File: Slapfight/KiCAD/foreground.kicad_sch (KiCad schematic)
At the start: 27 parts, among them U2D 74LS374, U3B_? 74LS00, U3C_ 74LS86, U3D_ 74LS04, U3F 74LS157, U3G 74LS157, U3H 74LS157, U4B_ 74LS32, U4B_? 74LS32, U4C_ 74LS10, U4D 74LS157, U4F RAM_2016, U4G RAM_2016, U4H 74LS174, U4J 74LS245, U6&7D 74LS194, U6D 74LS194, U6F 27C64 - A77-04, U6G 27C64 - A77-03, U6H_ 74LS32, U6J 74LS245, U7D 74LS194, U7E 74LS194, U7F 74LS157

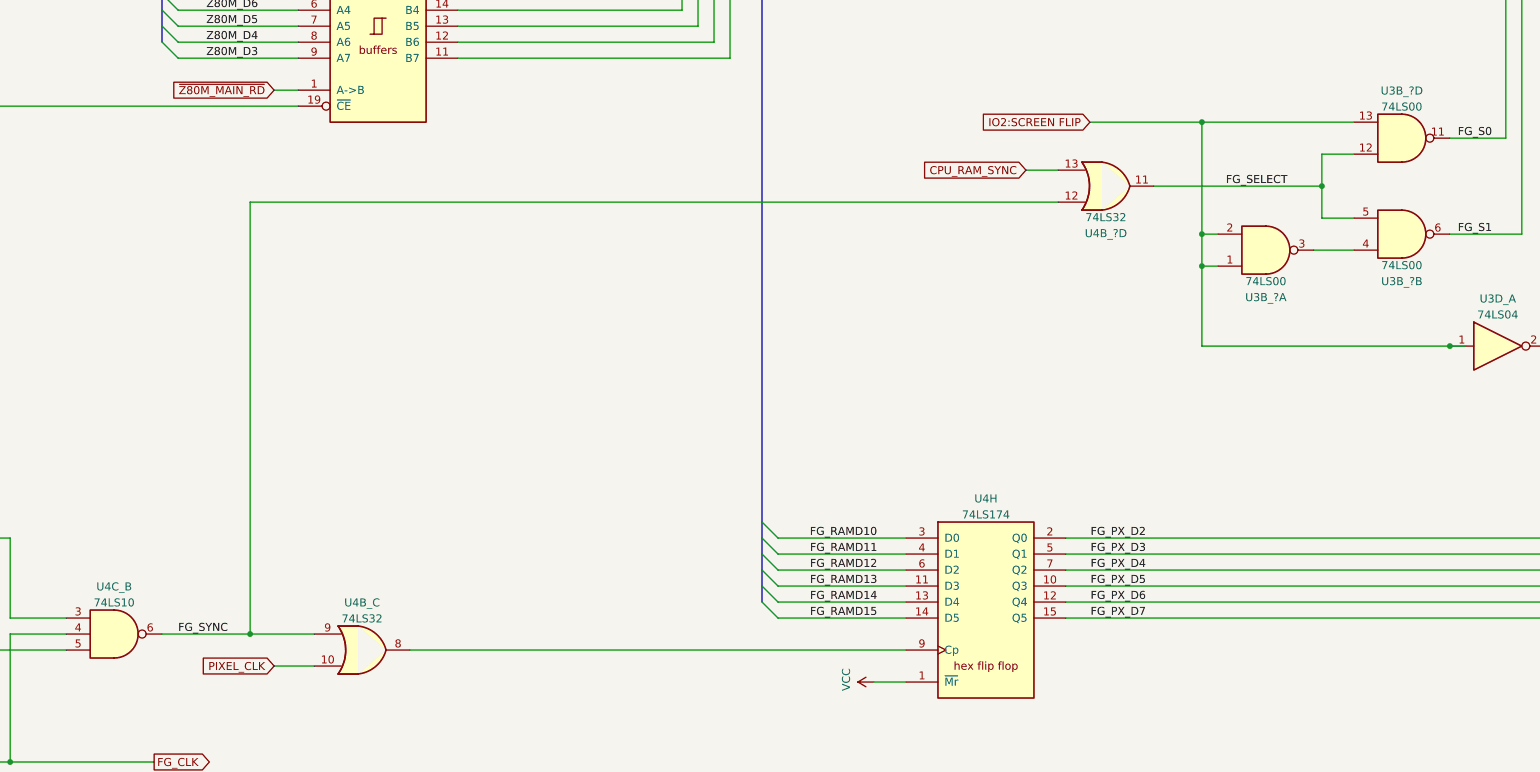
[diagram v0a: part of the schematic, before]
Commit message: Component naming updates
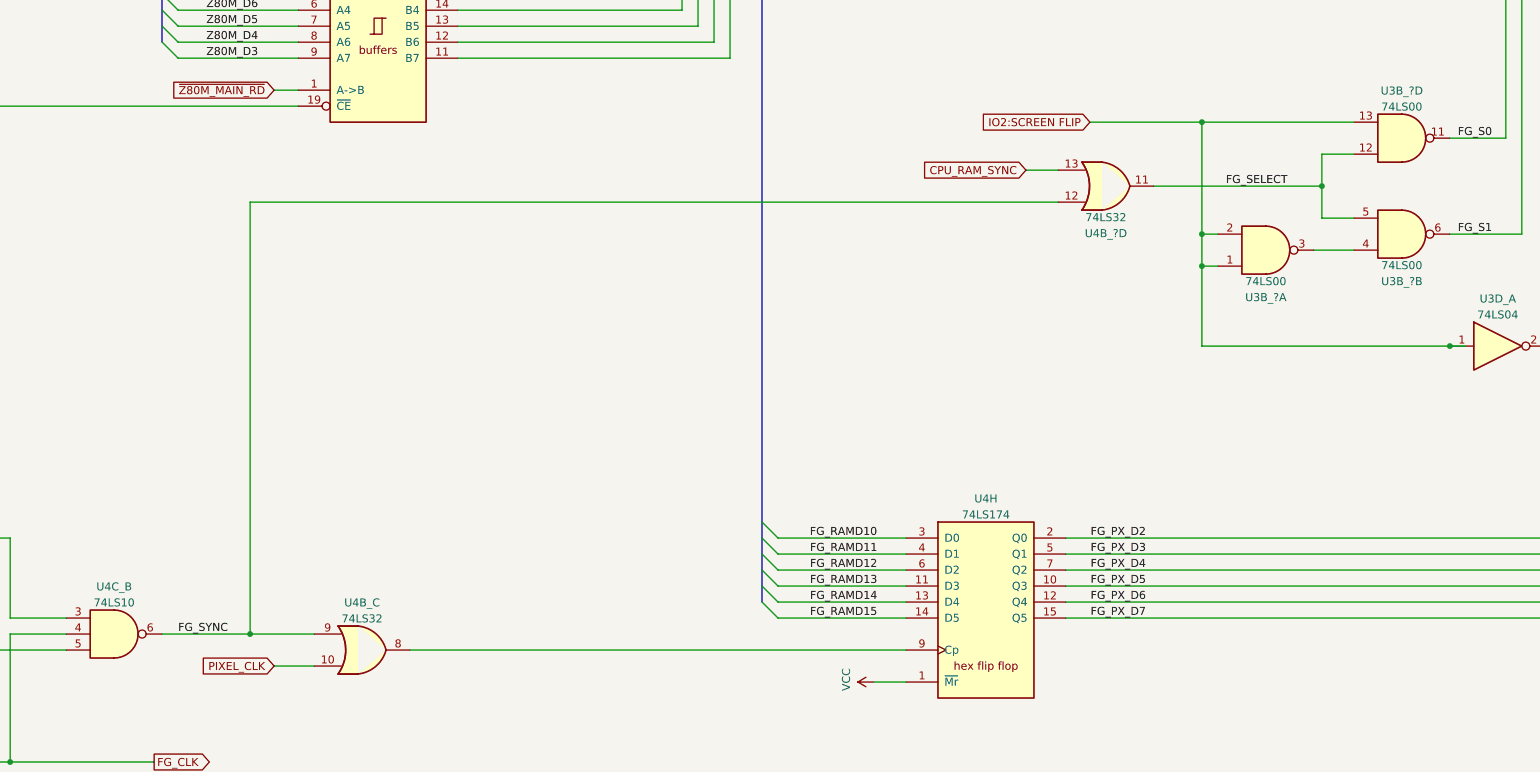
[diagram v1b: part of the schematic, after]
